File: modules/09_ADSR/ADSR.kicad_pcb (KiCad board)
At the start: 2 copper layers, 160 x 100 mm, 63 parts, among them IC1 µA741C, IC2 µA741C, IC3 µA741C, IC4 µA741C, IC5 µA741C, J1 BUS CONNECTOR, J2 EOS, J3 GND, J4 GND, P1 1M, P2 1M, P3 1M, P4 10k, P5 25k, T1 TUN, T2 TUN, T3 TUN, T4 TUN, T5 TUN, T6 TUN

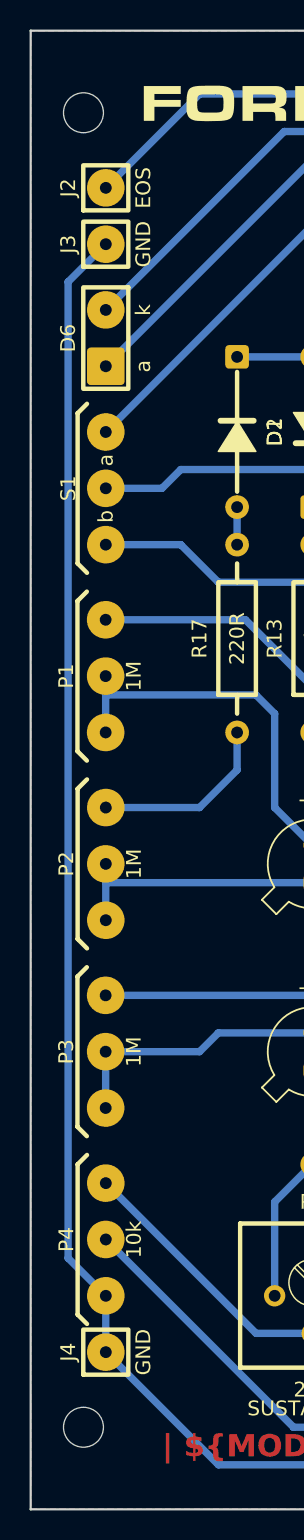
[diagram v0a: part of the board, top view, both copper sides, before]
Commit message: fixed card bracket footprint
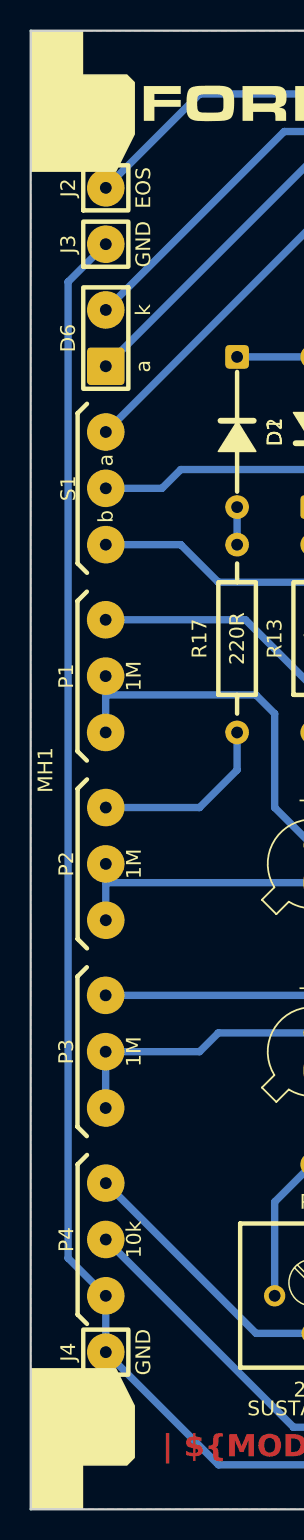
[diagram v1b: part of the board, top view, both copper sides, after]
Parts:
- removed MH2: MountingHole_2.7mm_M2.5_DIN965, MountingHole:MountingHole_2.7mm_M2.5_DIN965
- MH1: value MountingHole_2.7mm_M2.5_DIN965 -> CardBracket; footprint MountingHole:MountingHole_2.7mm_M2.5_DIN965 -> FormantKO:Card_Bracket
- moved MH1 44.6 mm to (55.0, 95.0)

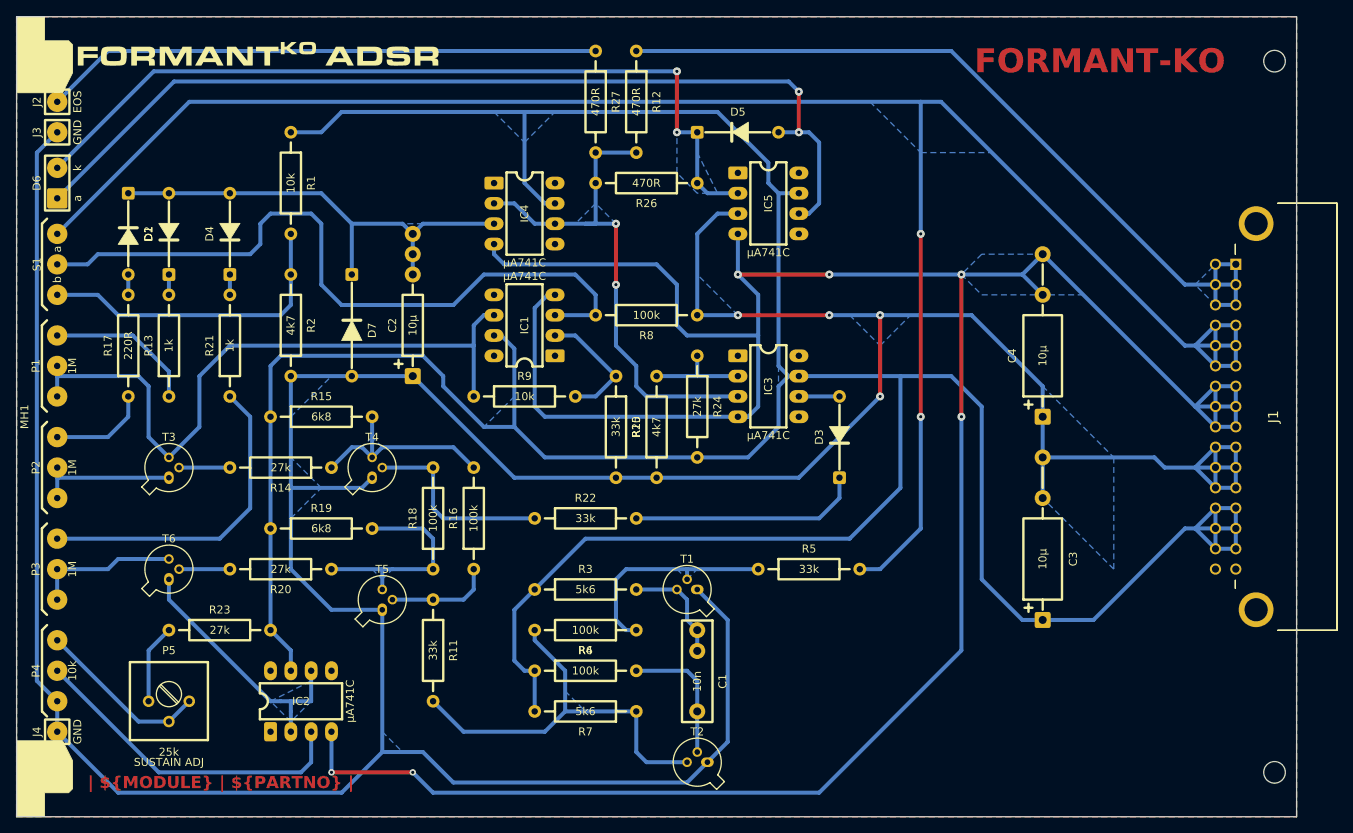
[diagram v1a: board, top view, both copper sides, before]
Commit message: adsr routing
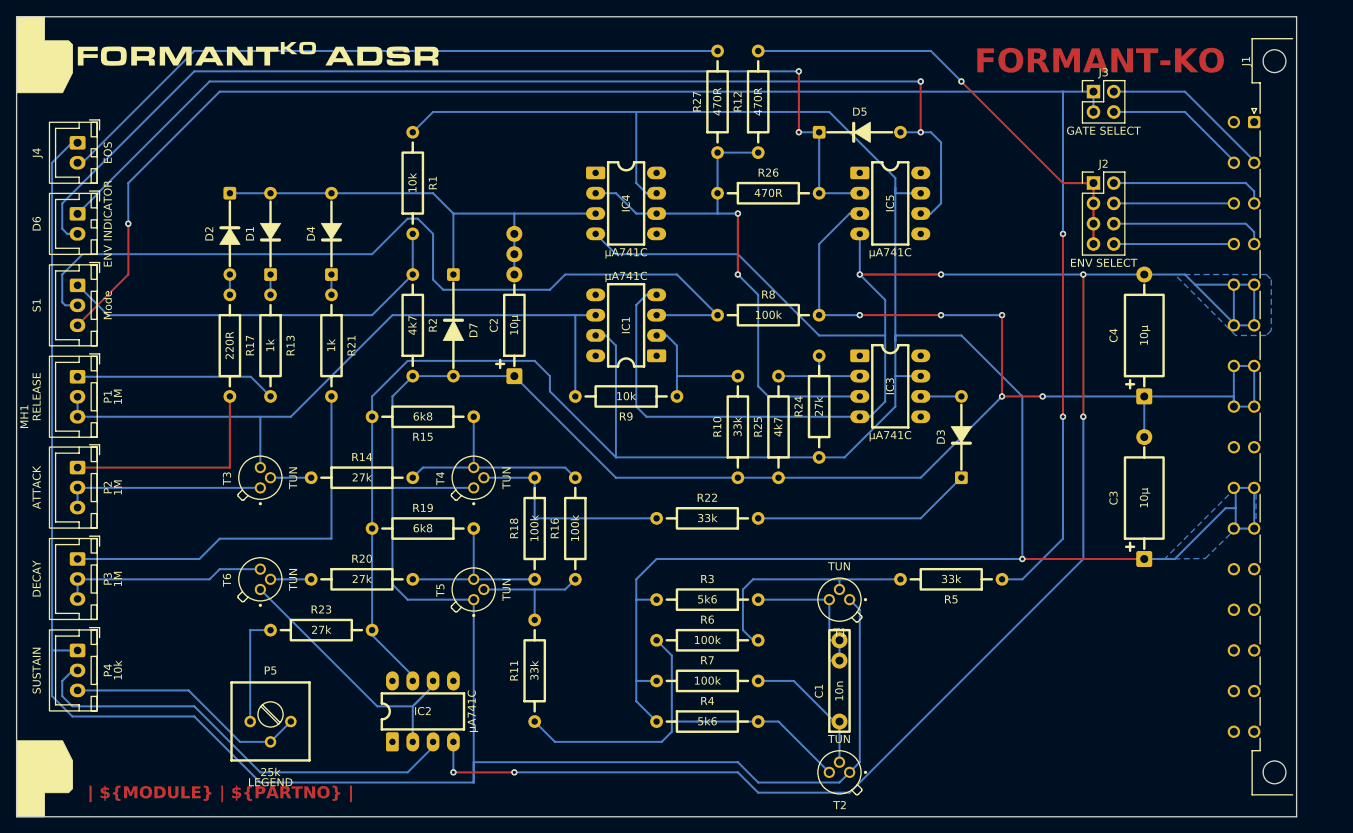
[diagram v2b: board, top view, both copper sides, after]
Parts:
- removed MH3, MH4: MountingHole_2.7mm_M2.5_DIN965, MountingHole:MountingHole_2.7mm_M2.5_DIN965
- C3, C4: footprint FormantKO:CP_Axial_600_800 -> FormantKO:CP_Axial_600
- D6: value Panel_LED -> ENV INDICATOR; footprint FormantKO:LED_Panel_Narrow -> FormantKO:Panel_Connector_1x02
- J1: value BUS CONNECTOR -> CardConnector; footprint FormantKO:DIN_Male -> FormantKO:Card_Connector
- J2: value EOS -> ENV SELECT; footprint FormantKO:Wire_1x01_General -> Connector_PinHeader_2.54mm:PinHeader_2x04_P2.54mm_Vertical
- J3: value GND -> GATE SELECT; footprint FormantKO:Wire_1x01_General -> Connector_PinHeader_2.54mm:PinHeader_2x02_P2.54mm_Vertical
- J4: value GND -> EOS; footprint FormantKO:Wire_1x01_General -> FormantKO:Panel_Connector_1x02
- P1, P2, P3, P4: footprint FormantKO:Potentiometer_Inline_Narrow -> FormantKO:Panel_Connector_1x03
- S1: value ~ -> Mode; footprint FormantKO:Switch_SPDT_Narrow -> FormantKO:Panel_Connector_1x03
- T1, T2, T3, T4, T5, T6: footprint FormantKO:TUN -> FormantKO:TO-18
- moved J2 129.9 mm to (189.6, 65.8), turned to 0 degrees
- moved J3 129.6 mm to (189.6, 54.4), turned to 0 degrees
- moved J4 72.4 mm to (62.6, 62.0), turned to -90 degrees
- moved J1 20.5 mm to (215.0, 95.0), turned to 0 degrees
- moved R5 17.8 mm to (171.8, 115.3), turned to 180 degrees
- moved T1 17.8 mm to (157.9, 117.9)
- moved C1 17.8 mm to (157.9, 129.3), turned to 90 degrees
- moved T2 16.6 mm to (157.9, 139.4)
- moved IC2 15.3 mm to (102.0, 135.6)
- moved R26 15.3 mm to (149.0, 67.1), turned to 0 degrees
- moved R4 15.3 mm to (141.3, 128.0), turned to 180 degrees
- moved R3 15.3 mm to (141.3, 117.9), turned to 180 degrees
- moved R6 15.3 mm to (141.3, 122.9), turned to 0 degrees
- moved R7 15.3 mm to (141.3, 133.1), turned to 0 degrees
- moved D5 15.2 mm to (160.4, 59.4)
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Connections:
- J2 pad 1: EOS -> ENV
- J3 pad 1: GND -> GATE
- P1 pad 1: Net-(T3-C) -> Net-(P1-Pad1)
- P1 pad 3: Net-(P1-Pad3) -> Net-(T3-C)
- P2 pad 1: Net-(T3-E) -> Net-(P2-Pad1)
- P2 pad 3: Net-(P2-Pad3) -> Net-(T3-E)
- P3 pad 1: Net-(T6-C) -> Net-(P3-Pad1)
- P3 pad 3: Net-(P3-Pad3) -> Net-(T6-C)
- P5 pad 1: Net-(P5-Pad1) -> Net-(P4-Pad3)
- P5 pad 3: Net-(P4-Pad3) -> Net-(P5-Pad3)
- R1 pad 1: +15V -> Net-(S1-a)
- R1 pad 2: Net-(S1-a) -> +15V
- R10 pad 1: Net-(IC1--) -> GND
- R10 pad 2: GND -> Net-(IC1--)
- R11 pad 1: Net-(T5-B) -> Net-(T2-C)
- R11 pad 2: Net-(T2-C) -> Net-(T5-B)
- R12 pad 1: ENV -> Net-(IC3-+)
- R12 pad 2: Net-(IC3-+) -> ENV
- R13 pad 1: Net-(P1-Pad3) -> Net-(D1-K)
- R13 pad 2: Net-(D1-K) -> Net-(P1-Pad1)
- R14 pad 1: Net-(T4-C) -> Net-(T3-B)
- R14 pad 2: Net-(T3-B) -> Net-(T4-C)
- R15 pad 1: +15V -> Net-(T4-C)
- R15 pad 2: Net-(T4-C) -> +15V
- R16 pad 1: Net-(T5-B) -> Net-(T4-C)
- R16 pad 2: Net-(T4-C) -> Net-(T5-B)
- R17 pad 1: Net-(P2-Pad3) -> Net-(D2-A)
- R17 pad 2: Net-(D2-A) -> Net-(P2-Pad1)
- R18 pad 1: Net-(T5-C) -> Net-(T4-B)
- R18 pad 2: Net-(T4-B) -> Net-(T5-C)
- R19 pad 1: +15V -> Net-(T5-C)
- R19 pad 2: Net-(T5-C) -> +15V
- R2 pad 1: Net-(S1-a) -> GND
- R2 pad 2: GND -> Net-(S1-a)
- R20 pad 1: Net-(T5-C) -> Net-(T6-B)
- R20 pad 2: Net-(T6-B) -> Net-(T5-C)
- R21 pad 1: Net-(P3-Pad3) -> Net-(D4-K)
- R21 pad 2: Net-(D4-K) -> Net-(P3-Pad1)
- R22 pad 1: Net-(T4-B) -> Net-(D3-K)
- R22 pad 2: Net-(D3-K) -> Net-(T4-B)
- R23 pad 1: Net-(P5-Pad1) -> Net-(P5-Pad3)
- R24 pad 1: Net-(IC3--) -> +15V
- R24 pad 2: +15V -> Net-(IC3--)
- R26 pad 1: Net-(D5-K) -> Net-(IC3-+)
- R26 pad 2: Net-(IC3-+) -> Net-(D5-K)
- R27 pad 1: EOS -> Net-(IC3-+)
- R27 pad 2: Net-(IC3-+) -> EOS
- R3 pad 1: +15V -> Net-(T1-C)
- R3 pad 2: Net-(T1-C) -> +15V
- R4 pad 1: +15V -> Net-(T2-B)
- R4 pad 2: Net-(T2-B) -> +15V
- R5 pad 1: Net-(T1-B) -> GATE
- R5 pad 2: GATE -> Net-(T1-B)
- R6 pad 1: Net-(T1-B) -> Net-(T2-C)
- R6 pad 2: Net-(T2-C) -> Net-(T1-B)
- R7 pad 1: Net-(T2-C) -> +15V
- R7 pad 2: +15V -> Net-(T2-C)
- R8 pad 1: GND -> Net-(IC1-+)
- R8 pad 2: Net-(IC1-+) -> GND
- R9 pad 1: Net-(T3-C) -> Net-(IC1--)
- R9 pad 2: Net-(IC1--) -> Net-(T3-C)
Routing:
- net Net-(P3-Pad1): track 0.00 -> 50.6 mm
- net ENV: track 102.3 -> 56.4 mm, vias 0 -> 1
- net Net-(P3-Pad3): track 40.7 -> 0.00 mm
- net GATE: track 252.3 -> 213.9 mm, vias 2 -> 3
- net -15V: track 345.1 -> 312.6 mm
- net +15V: track 429.4 -> 400.3 mm, vias 0 -> 1
- net Net-(P2-Pad1): track 0.00 -> 27.9 mm
- net Net-(P1-Pad1): track 0.00 -> 25.1 mm
- net Net-(D5-K): track 104.6 -> 127.1 mm
- net GATE1: track 0.00 -> 21.1 mm
- net ENV3: track 0.00 -> 19.5 mm
- net ENV1: track 0.00 -> 19.5 mm
- net Net-(P1-Pad3): track 18.9 -> 0.00 mm
- net GATE2: track 0.00 -> 17.5 mm
- net Net-(IC1-+): track 90.9 -> 107.9 mm
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- removed copper zone on B.Cu, net ENV
- removed copper zone on B.Cu, net GATE
- removed copper zone on B.Cu, net GND
- removed copper zone on F.Cu, net GND
- removed copper zone on B.Cu, net Net-(D1-A)
- removed copper zone on B.Cu, net Net-(D5-K)
- removed copper zone on B.Cu, net Net-(IC2--)
- removed copper zone on B.Cu, net Net-(IC3-+)
- removed copper zone on B.Cu, net Net-(T1-B)
- removed copper zone on B.Cu, net Net-(T2-C)
- removed copper zone on B.Cu, net Net-(T4-C)
- removed copper zone on B.Cu, net Net-(T5-C)
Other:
- board text removed: "Mounting holes are optional Keepout areas are for for guide rails"

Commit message: adsr pcb
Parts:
- D6: value ENV INDICATOR -> ENV IND
- S1: value Mode -> MODE
- moved IC1 5.39 mm to (131.2, 83.6)
- moved IC3 5.39 mm to (164.2, 91.2)
- moved IC4 5.39 mm to (131.2, 68.3)
- moved IC5 5.39 mm to (164.2, 68.3)
- moved IC2 5.39 mm to (105.8, 131.8)
- moved R3 2.54 mm to (141.3, 115.3)
- moved R4 2.54 mm to (141.3, 125.5)
- moved T1 2.54 mm to (157.9, 115.3)
- moved C1 2.54 mm to (157.9, 126.8)
- moved C3 2.54 mm to (196.0, 102.6)
- moved R5 2.54 mm to (171.8, 112.8)
- moved R6 2.54 mm to (141.3, 120.4)
- moved R7 2.54 mm to (141.3, 130.6)
- moved T2 2.54 mm to (157.9, 136.9)
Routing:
- net -15V: track 312.6 -> 304.0 mm
- net GND: track 458.3 -> 451.5 mm
- net +15V: track 400.3 -> 393.9 mm
- net ENV: track 56.4 -> 61.8 mm
- net Net-(P2-Pad1): track 27.9 -> 22.7 mm
- net Net-(T1-C): track 21.6 -> 17.0 mm
- net Net-(P3-Pad1): track 50.6 -> 46.1 mm
- net Net-(T4-B): track 26.7 -> 23.7 mm
- net Net-(IC2--): track 35.6 -> 33.1 mm
- net GATE: track 213.9 -> 211.8 mm
- net Net-(P5-Pad3): track 14.0 -> 12.5 mm
- net Net-(IC3-+): track 67.4 -> 65.9 mm
- net Net-(IC2-+): track 56.7 -> 55.4 mm
- net Net-(T2-C): track 53.3 -> 54.3 mm
- net Net-(T1-B): track 29.0 -> 28.0 mm
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- added copper zone on B.Cu, net GATE
- added copper zone on B.Cu, net GND
- added copper zone on F.Cu, net GND
- added copper zone on B.Cu, net Net-(D1-A)
- added copper zone on B.Cu, net Net-(D5-K)
- added copper zone on B.Cu, net Net-(IC1-+)
- added copper zone on B.Cu, net Net-(IC1--)
- added copper zone on B.Cu, net Net-(IC2--)
- added copper zone on B.Cu, net Net-(IC3-+)
- added copper zone on B.Cu, net Net-(IC3--)
- added copper zone on B.Cu, net Net-(T1-B)
- added copper zone on B.Cu, net Net-(T3-C)
- added copper zone on B.Cu, net Net-(T4-C)
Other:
- board text added: "ENV1"
- board text added: "ENV2"
- board text added: "ENV3"
- board text added: "ENV4"
- board text added: "GATE1"
- board text added: "GATE2"
